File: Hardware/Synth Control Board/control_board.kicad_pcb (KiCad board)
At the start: 2 copper layers, 127 x 177.8 mm, 53 parts, among them J1 Conn_01x13, J10 Conn_01x05, J11 Conn_01x08, J12 Conn_01x06, J2 Conn_01x03, J3 Conn_01x13, J4 Conn_01x13, J5 Conn_01x02, J6 Conn_01x13, J7 Conn_01x05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

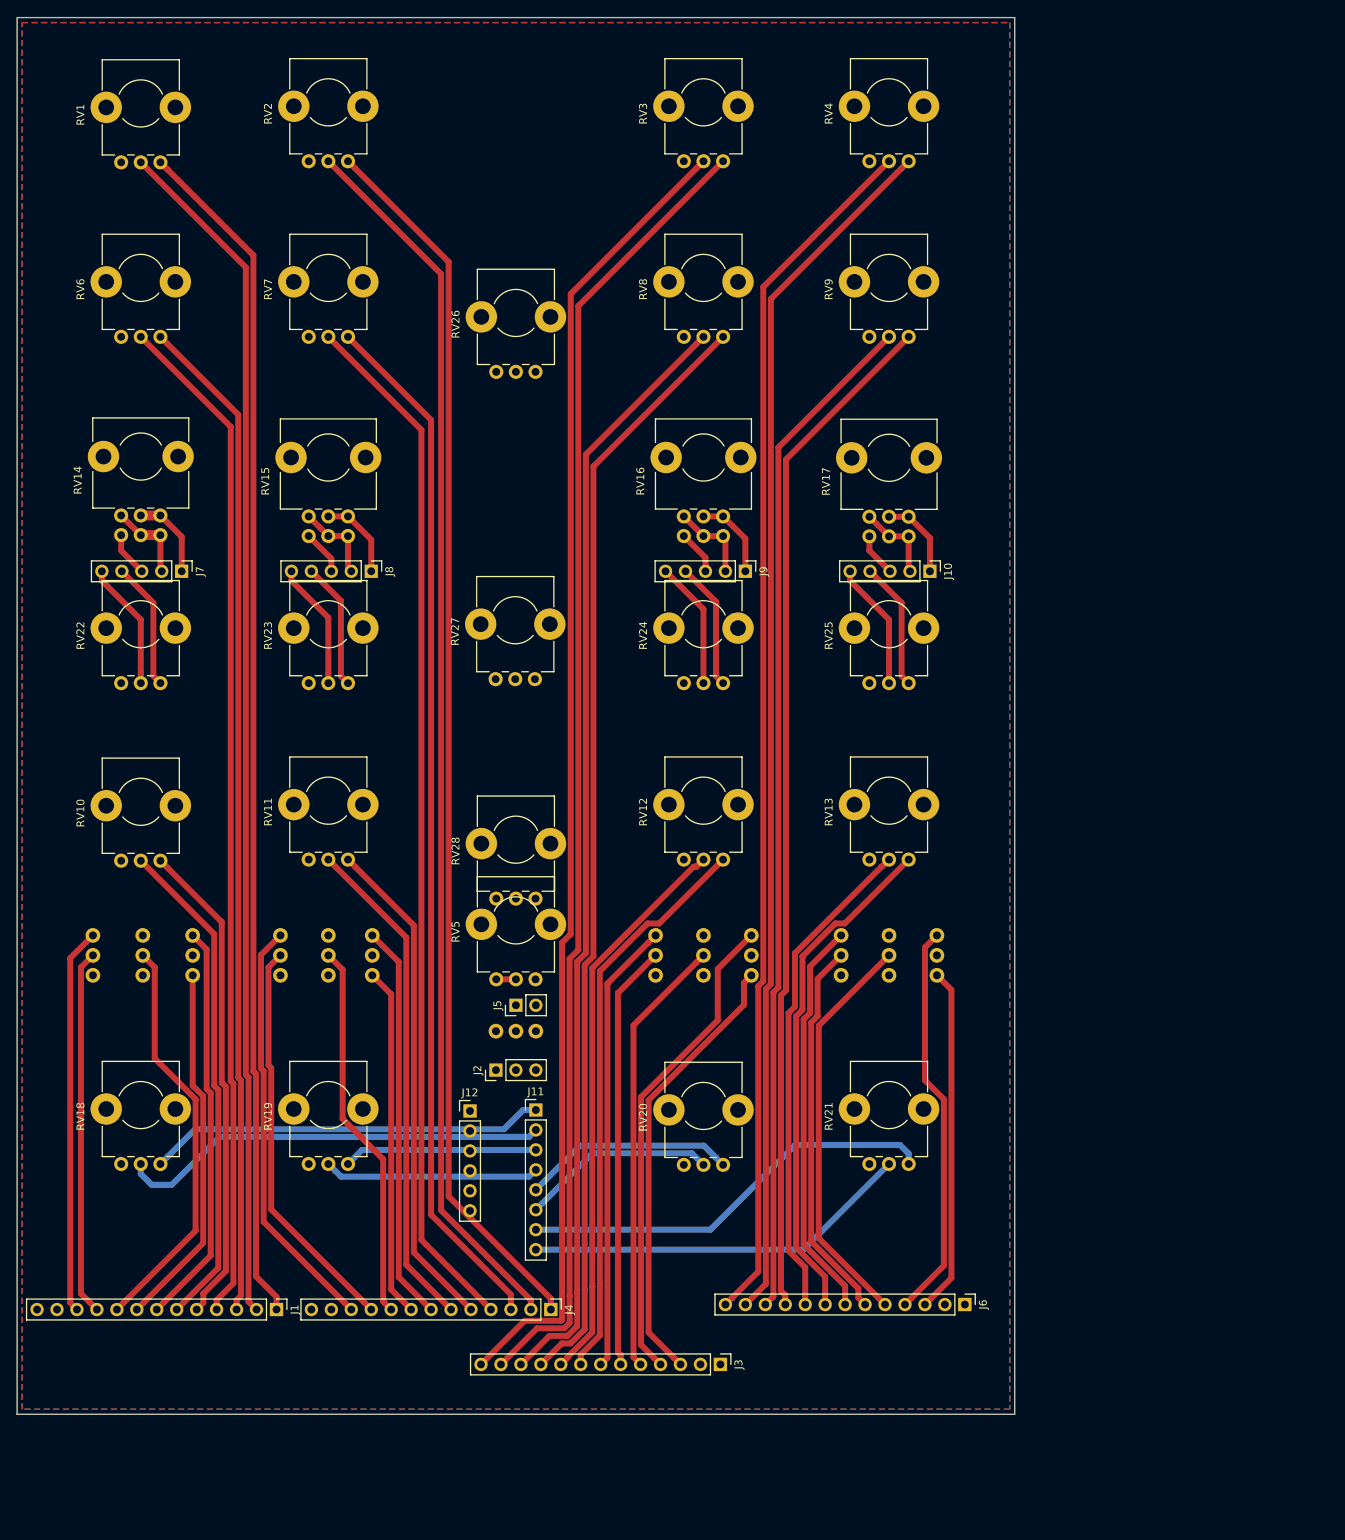
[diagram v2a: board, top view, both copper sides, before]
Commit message: add mounting holes to control board PCB
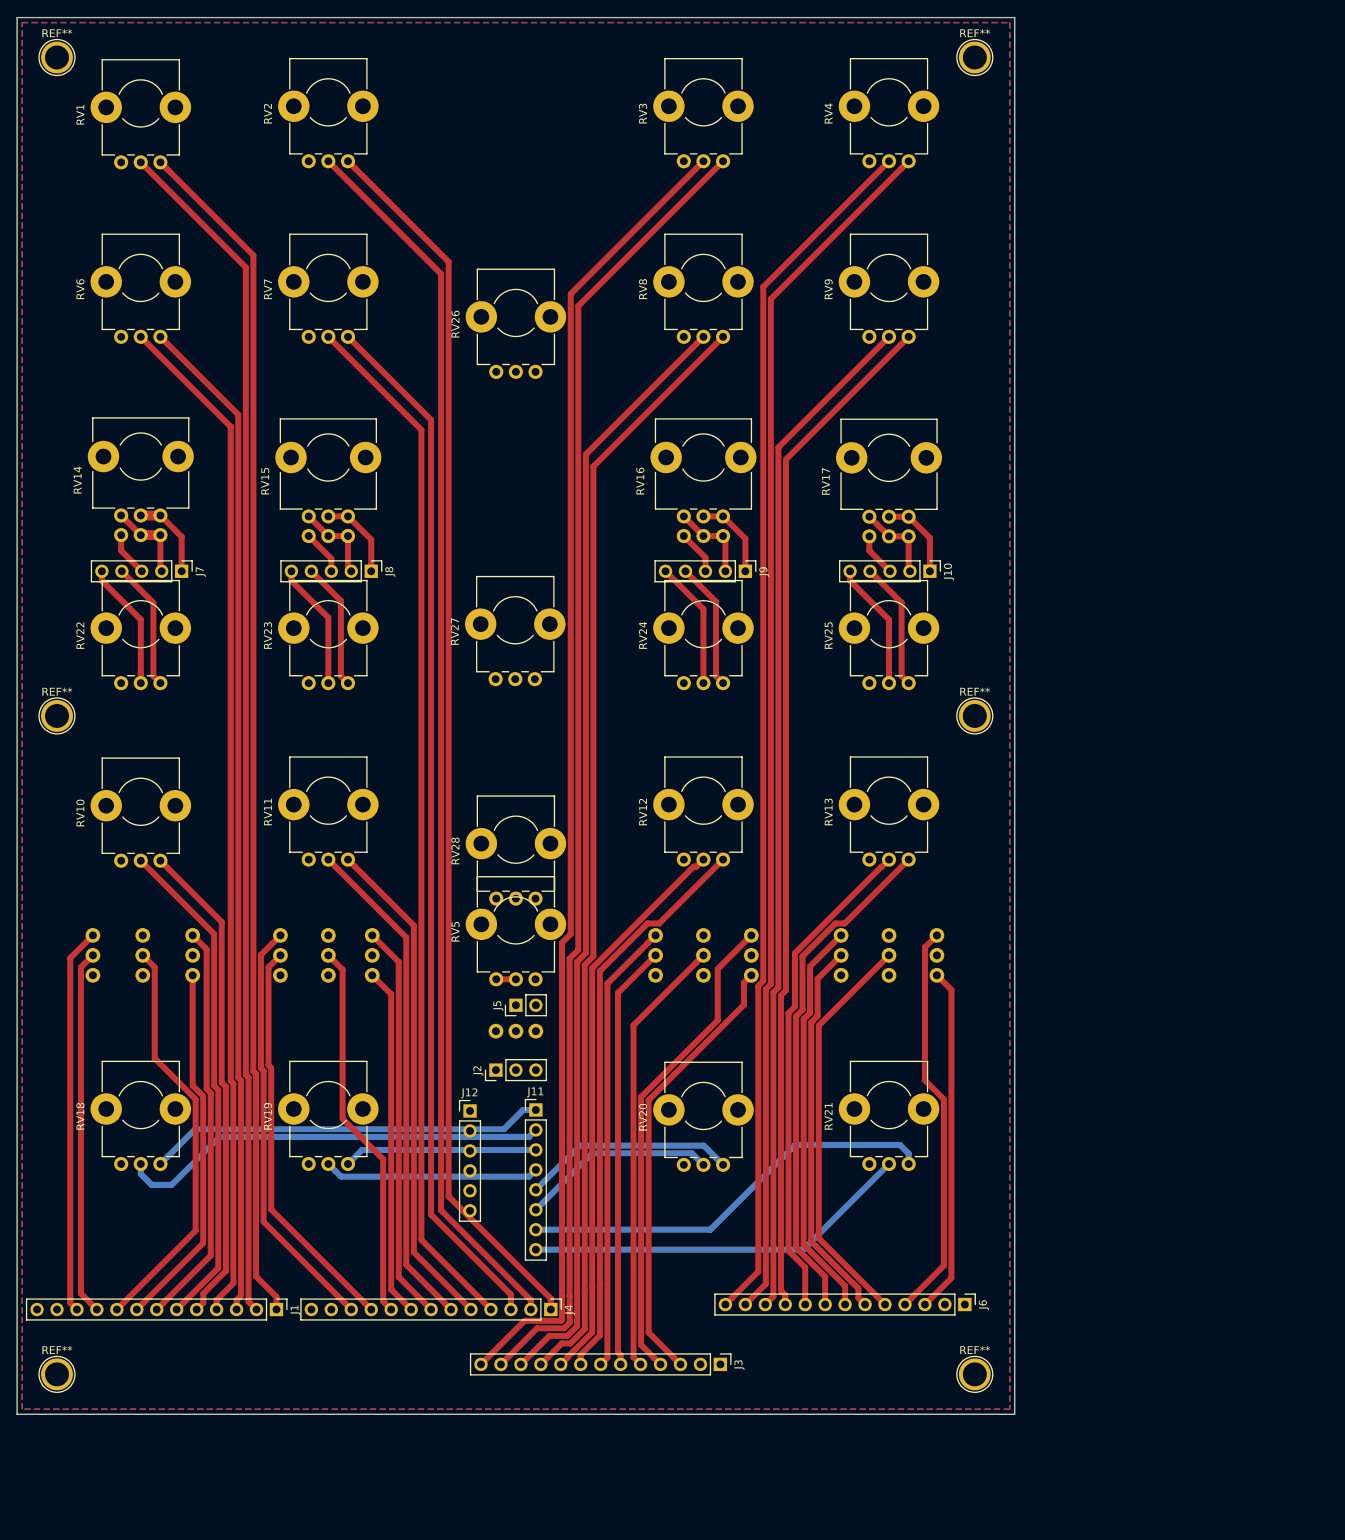
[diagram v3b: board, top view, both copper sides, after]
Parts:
- added REF**: 1pin, Connectors:1pin, F.Cu at (5.08, 88.9)
- added REF**: 1pin, Connectors:1pin, F.Cu at (121.9, 88.9)
- added REF**: 1pin, Connectors:1pin, F.Cu at (121.9, 5.08)
- added REF**: 1pin, Connectors:1pin, F.Cu at (5.08, 5.08)
- added REF**: 1pin, Connectors:1pin, F.Cu at (121.9, 172.7)
- added REF**: 1pin, Connectors:1pin, F.Cu at (5.08, 172.7)
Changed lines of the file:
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@@
 (kicad_pcb (version 4) (host pcbnew 4.0.7)
   (general
-    (links 145)
-    (no_connects 18)
-    (area -0.075001 -0.075001 127.075001 177.875001)
+    (links 0)
+    (no_connects 22)
+    (area -0.765 -0.075001 127.075001 177.875001)
     (thickness 1.6)
     (drawings 4)
     (tracks 366)
     (zones 0)
-    (modules 53)
+    (modules 59)
     (nets 74)
   )
@@
     (add_net GND)
   )
+  (module Connectors:1pin (layer F.Cu)
+    (at 5.08 88.9)
+    (descr "module 1 pin (ou trou mecanique de percage)")
+    (tags DEV)
+    (fp_text reference REF** (at 0 -3.048) (layer F.SilkS)
+      (effects (font (size 1 1) (thickness 0.15)))
+    )
+    (fp_text value 1pin (at 0 3) (layer F.Fab)
+      (effects (font (size 1 1) (thickness 0.15)))
+    )
+    (fp_circle (center 0 0) (end 2 0.8) (layer F.Fab) (width 0.1))
+    (fp_circle (center 0 0) (end 2.6 0) (layer F.CrtYd) (width 0.05))
+    (fp_circle (center 0 0) (end 0 -2.286) (layer F.SilkS) (width 0.12))
+    (pad 1 thru_hole circle (at 0 0) (size 4.064 4.064) (drill 3.048) (layers *.Cu *.Mask))
+  )
+  (module Connectors:1pin (layer F.Cu)
+    (at 121.92 88.9)
+    (descr "module 1 pin (ou trou mecanique de percage)")
+    (tags DEV)
+    (fp_text reference REF** (at 0 -3.048) (layer F.SilkS)
+      (effects (font (size 1 1) (thickness 0.15)))
+    )
+    (fp_text value 1pin (at 0 3) (layer F.Fab)
+      (effects (font (size 1 1) (thickness 0.15)))
+    )
+    (fp_circle (center 0 0) (end 2 0.8) (layer F.Fab) (width 0.1))
+    (fp_circle (center 0 0) (end 2.6 0) (layer F.CrtYd) (width 0.05))
+    (fp_circle (center 0 0) (end 0 -2.286) (layer F.SilkS) (width 0.12))
+    (pad 1 thru_hole circle (at 0 0) (size 4.064 4.064) (drill 3.048) (layers *.Cu *.Mask))
+  )
+  (module Connectors:1pin (layer F.Cu)
+    (at 121.92 5.08)
+    (descr "module 1 pin (ou trou mecanique de percage)")
+    (tags DEV)
+    (fp_text reference REF** (at 0 -3.048) (layer F.SilkS)
+      (effects (font (size 1 1) (thickness 0.15)))
+    )
+    (fp_text value 1pin (at 0 3) (layer F.Fab)
+      (effects (font (size 1 1) (thickness 0.15)))
+    )
+    (fp_circle (center 0 0) (end 2 0.8) (layer F.Fab) (width 0.1))
+    (fp_circle (center 0 0) (end 2.6 0) (layer F.CrtYd) (width 0.05))
+    (fp_circle (center 0 0) (end 0 -2.286) (layer F.SilkS) (width 0.12))
+    (pad 1 thru_hole circle (at 0 0) (size 4.064 4.064) (drill 3.048) (layers *.Cu *.Mask))
+  )
+  (module Connectors:1pin (layer F.Cu)
+    (at 5.08 5.08)
+    (descr "module 1 pin (ou trou mecanique de percage)")
+    (tags DEV)
+    (fp_text reference REF** (at 0 -3.048) (layer F.SilkS)
+      (effects (font (size 1 1) (thickness 0.15)))
+    )
+    (fp_text value 1pin (at 0 3) (layer F.Fab)
+      (effects (font (size 1 1) (thickness 0.15)))
+    )
+    (fp_circle (center 0 0) (end 2 0.8) (layer F.Fab) (width 0.1))
+    (fp_circle (center 0 0) (end 2.6 0) (layer F.CrtYd) (width 0.05))
+    (fp_circle (center 0 0) (end 0 -2.286) (layer F.SilkS) (width 0.12))
+    (pad 1 thru_hole circle (at 0 0) (size 4.064 4.064) (drill 3.048) (layers *.Cu *.Mask))
+  )
+  (module Connectors:1pin (layer F.Cu)
+    (at 121.92 172.72)
+    (descr "module 1 pin (ou trou mecanique de percage)")
+    (tags DEV)
+    (fp_text reference REF** (at 0 -3.048) (layer F.SilkS)
+      (effects (font (size 1 1) (thickness 0.15)))
+    )
+    (fp_text value 1pin (at 0 3) (layer F.Fab)
+      (effects (font (size 1 1) (thickness 0.15)))
+    )
+    (fp_circle (center 0 0) (end 2 0.8) (layer F.Fab) (width 0.1))
+    (fp_circle (center 0 0) (end 2.6 0) (layer F.CrtYd) (width 0.05))
+    (fp_circle (center 0 0) (end 0 -2.286) (layer F.SilkS) (width 0.12))
+    (pad 1 thru_hole circle (at 0 0) (size 4.064 4.064) (drill 3.048) (layers *.Cu *.Mask))
+  )
   (module Potentiometers:Potentiometer_Bourns_PTV09A-1_Horizontal (layer F.Cu)
     (at 18.248 107.33 90)
@@
     )
   )
+  (module Connectors:1pin (layer F.Cu)
+    (at 5.08 172.72)
+    (descr "module 1 pin (ou trou mecanique de percage)")
+    (tags DEV)
+    (fp_text reference REF** (at 0 -3.048) (layer F.SilkS)
+      (effects (font (size 1 1) (thickness 0.15)))
+    )
+    (fp_text value 1pin (at 0 3) (layer F.Fab)
+      (effects (font (size 1 1) (thickness 0.15)))
+    )
+    (fp_circle (center 0 0) (end 2 0.8) (layer F.Fab) (width 0.1))
+    (fp_circle (center 0 0) (end 2.6 0) (layer F.CrtYd) (width 0.05))
+    (fp_circle (center 0 0) (end 0 -2.286) (layer F.SilkS) (width 0.12))
+    (pad 1 thru_hole circle (at 0 0) (size 4.064 4.064) (drill 3.048) (layers *.Cu *.Mask))
+  )
   (gr_line (start 127 0) (end 0 0) (layer Edge.Cuts) (width 0.15))
